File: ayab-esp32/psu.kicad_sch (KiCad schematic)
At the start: 45 parts, among them J602 Brother_5P, J604 Brother_4R, U401 XL1509, U402 XL1509

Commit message: Fix U602 3.3V regulator metadata [skip ci]
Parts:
- U402: LCSC ID C61063 -> C74193; OEM PN XL1509-5.0E1 -> XL1509-3.3E1
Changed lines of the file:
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@@
       (effects (font (size 1.27 1.27)) hide)
     )
-    (property "Datasheet" "https://datasheet.lcsc.com/lcsc/2304140030_XLSEMI-XL1509-5-0E1_C61063.pdf" (at 201.93 128.27 0)
+    (property "Datasheet" "https://www.lcsc.com/product-detail/C74193.html" (at 201.93 128.27 0)
       (effects (font (size 1.27 1.27)) hide)
     )
@@
       (effects (font (size 1.27 1.27)) hide)
     )
-    (property "LCSC ID" "C61063" (at 201.93 128.27 0)
+    (property "LCSC ID" "C74193" (at 201.93 128.27 0)
       (effects (font (size 1.27 1.27)) hide)
     )
-    (property "OEM PN" "XL1509-5.0E1" (at 201.93 128.27 0)
+    (property "OEM PN" "XL1509-3.3E1" (at 201.93 128.27 0)
       (effects (font (size 1.27 1.27)) hide)
     )

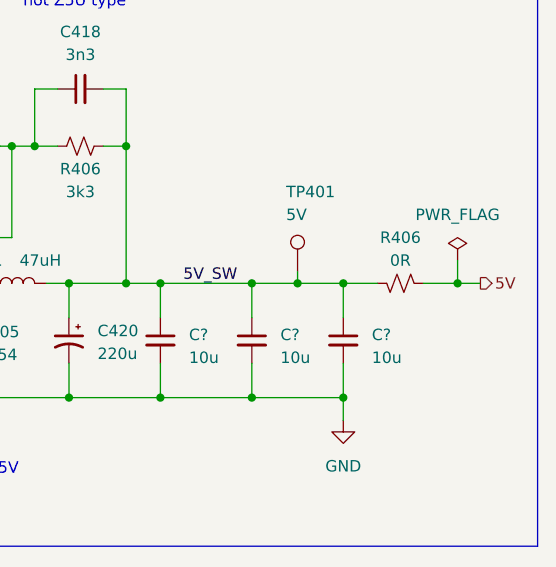
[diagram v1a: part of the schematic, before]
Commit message: Add LM66100 machine 5V reverse-current isolation
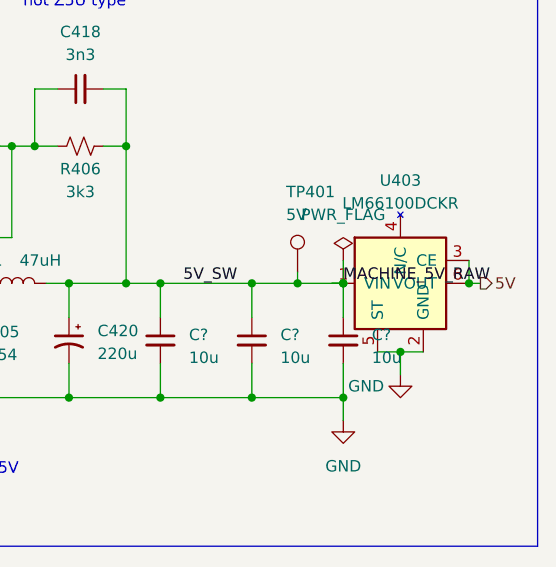
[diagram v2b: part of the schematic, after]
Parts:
- removed R406: 0R, Resistor_SMD:R_0603_1608Metric, symbol ayab-lib:R_Small_US
- added U403: LM66100DCKR, Package_TO_SOT_SMD:SOT-363_SC-70-6, symbol ayab-lib:LM66100
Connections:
- net 5V: now also U403.3 (CE), U403.6 (VOUT)
- net 5V_SW: now also U403.1 (VIN)
- net GND: now also U403.2 (GND), U403.5 (ST)
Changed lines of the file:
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@@
   )
   (junction (at 252.73 54.61) (diameter 0) (color 0 0 0 0)
-  )
-  (junction (at 270.51 54.61) (diameter 0) (color 0 0 0 0)
-  )
-  (junction (at 48.26 119.38) (diameter 0) (color 0 0 0 0)
+  )  (junction (at 48.26 119.38) (diameter 0) (color 0 0 0 0)
   )
   (junction (at 175.26 140.97) (diameter 0) (color 0 0 0 0)
@@
     (stroke (width 0) (type default))
   )
+  (wire (pts (xy 257.81 54.61) (xy 256.54 54.61))
+    (stroke (width 0) (type default))
+  )
+  (wire (pts (xy 257.81 52.07) (xy 257.81 54.61))
+    (stroke (width 0) (type default))
+  )
+  (wire (pts (xy 271.78 54.61) (xy 273.05 54.61))
+    (stroke (width 0) (type default))
+  )
+  (wire (pts (xy 271.78 52.07) (xy 271.78 54.61))
+    (stroke (width 0) (type default))
+  )
+  (wire (pts (xy 261.62 62.23) (xy 264.16 62.23))
+    (stroke (width 0) (type default))
+  )
+  (wire (pts (xy 266.7 62.23) (xy 264.16 62.23))
+    (stroke (width 0) (type default))
+  )
+  (wire (pts (xy 264.16 62.23) (xy 264.16 64.77))
+    (stroke (width 0) (type default))
+  )
+  (junction (at 257.81 54.61) (diameter 0) (color 0 0 0 0)
+  )
+  (junction (at 271.78 54.61) (diameter 0) (color 0 0 0 0)
+  )
+  (junction (at 264.16 62.23) (diameter 0) (color 0 0 0 0)
+  )
+  (label "MACHINE_5V_RAW" (at 257.81 54.61 0) (fields_autoplaced)
+    (effects (font (size 1.27 1.27)) (justify left bottom))
+  )
   (wire (pts (xy 115.57 54.61) (xy 109.22 54.61))
     (stroke (width 0) (type default))
@@
   (wire (pts (xy 203.2 67.31) (xy 205.74 67.31))
     (stroke (width 0) (type default))
-  )
-  (wire (pts (xy 270.51 52.07) (xy 270.51 54.61))
-    (stroke (width 0) (type default))
-  )
-  (wire (pts (xy 233.68 54.61) (xy 237.49 54.61))
+  )  (wire (pts (xy 233.68 54.61) (xy 237.49 54.61))
     (stroke (width 0) (type default))
   )
@@
   (wire (pts (xy 44.45 68.58) (xy 44.45 69.85))
     (stroke (width 0) (type default))
-  )
-  (wire (pts (xy 270.51 54.61) (xy 273.05 54.61))
-    (stroke (width 0) (type default))
-  )
-  (wire (pts (xy 237.49 67.31) (xy 247.65 67.31))
+  )  (wire (pts (xy 237.49 67.31) (xy 247.65 67.31))
     (stroke (width 0) (type default))
   )
@@
   (wire (pts (xy 252.73 54.61) (xy 257.81 54.61))
     (stroke (width 0) (type default))
-  )
-  (wire (pts (xy 266.7 54.61) (xy 270.51 54.61))
-    (stroke (width 0) (type default))
-  )
-  (wire (pts (xy 110.49 120.65) (xy 110.49 123.19))
+  )  (wire (pts (xy 110.49 120.65) (xy 110.49 123.19))
     (stroke (width 0) (type default))
   )
@@
   (wire (pts (xy 110.49 113.03) (xy 110.49 115.57))
     (stroke (width 0) (type default))
-  )
-  (wire (pts (xy 257.81 54.61) (xy 261.62 54.61))
-    (stroke (width 0) (type default))
-  )
-  (wire (pts (xy 189.23 67.31) (xy 198.12 67.31))
+  )  (wire (pts (xy 189.23 67.31) (xy 198.12 67.31))
     (stroke (width 0) (type default))
   )
@@
     )
   )
-  (symbol (lib_id "ayab-lib:R_Small_US") (at 264.16 54.61 90) (mirror x) (unit 1)
-    (in_bom yes) (on_board yes) (dnp no)
-    (property "Reference" "R406" (at 264.16 49.53 90)
-      (effects (font (size 1.27 1.27)))
-    )
-    (property "Value" "0R" (at 264.16 52.07 90)
-      (effects (font (size 1.27 1.27)))
-    )
-    (property "Footprint" "Resistor_SMD:R_0603_1608Metric" (at 264.16 54.61 0)
-      (effects (font (size 1.27 1.27)) hide)
-    )
-    (property "Datasheet" "~" (at 264.16 54.61 0)
-      (effects (font (size 1.27 1.27)) hide)
-    )
-    (property "Package" "0603" (at 264.16 54.61 0)
-      (effects (font (size 1.27 1.27)) hide)
-    )
-    (property "LCSC ID" "C21189" (at 264.16 54.61 0)
-      (effects (font (size 1.27 1.27)) hide)
-    )
-    (property "OEM PN" "0603WAF0000T5E" (at 264.16 54.61 0)
-      (effects (font (size 1.27 1.27)) hide)
-    )
-    (property "OEM" "UNI-ROYAL(Uniroyal Elec)" (at 264.16 54.61 0)
-      (effects (font (size 1.27 1.27)) hide)
-    )
-    (pin "1")
-    (pin "2")
-    (instances
-      (project "electronic-knitter"
-        (path "/a3f4eded-ecb9-44ce-82ad-ad815e00f2c9/d37dfdc2-398a-4de1-8840-934586e4e3cf"
-          (reference "R406") (unit 1)
-        )
-      )
-      (project "ayab-esp32"
-        (path "/ad16b75f-afc8-4717-a7c6-8dd7b69a18e2/512b1de4-f8f4-4173-a7be-69b46f59a5e5"
-          (reference "R611") (unit 1)
-        )
-      )
-    )
-  )
   (symbol (lib_id "power:+3V3") (at 133.35 113.03 0) (unit 1)
     (in_bom yes) (on_board yes) (dnp no) (fields_autoplaced)
@@
     )
   )
-  (symbol (lib_id "power:PWR_FLAG") (at 270.51 52.07 0) (unit 1)
+  (symbol (lib_id "power:PWR_FLAG") (at 257.81 52.07 0) (unit 1)
     (in_bom yes) (on_board yes) (dnp no) (fields_autoplaced)
-    (property "Reference" "#FLG0605" (at 270.51 50.165 0)
+    (property "Reference" "#FLG0605" (at 257.81 50.165 0)
       (effects (font (size 1.27 1.27)) hide)
     )
-    (property "Value" "PWR_FLAG" (at 270.51 46.99 0)
+    (property "Value" "PWR_FLAG" (at 257.81 46.99 0)
       (effects (font (size 1.27 1.27)))
     )
-    (property "Footprint" "" (at 270.51 52.07 0)
+    (property "Footprint" "" (at 257.81 52.07 0)
       (effects (font (size 1.27 1.27)) hide)
     )
-    (property "Datasheet" "~" (at 270.51 52.07 0)
+    (property "Datasheet" "~" (at 257.81 52.07 0)
       (effects (font (size 1.27 1.27)) hide)
     )
@@
         )
       )
+    )
+  )
+  (symbol (lib_id "ayab-lib:LM66100") (at 264.16 54.61 0) (unit 1)
+    (in_bom yes) (on_board yes) (dnp no) (fields_autoplaced)
+    (property "Reference" "U403" (at 264.16 43.18 0)
+      (effects (font (size 1.27 1.27)))
+    )
+    (property "Value" "LM66100DCKR" (at 264.16 45.72 0)
+      (effects (font (size 1.27 1.27)))
+    )
+    (property "Footprint" "Package_TO_SOT_SMD:SOT-363_SC-70-6" (at 264.16 54.61 0)
+      (effects (font (size 1.27 1.27)) hide)
+    )
+    (property "Datasheet" "https://www.ti.com/lit/ds/symlink/lm66100.pdf" (at 264.16 54.61 0)
+      (effects (font (size 1.27 1.27)) hide)
+    )
+    (property "Package" "SC-70-6" (at 264.16 54.61 0)
+      (effects (font (size 1.27 1.27)) hide)
+    )
+    (property "LCSC ID" "C2869734" (at 264.16 54.61 0)
+      (effects (font (size 1.27 1.27)) hide)
+    )
+    (property "OEM PN" "LM66100DCKR" (at 264.16 54.61 0)
+      (effects (font (size 1.27 1.27)) hide)
+    )
+    (property "OEM" "Texas Instruments" (at 264.16 54.61 0)
+      (effects (font (size 1.27 1.27)) hide)
+    )
+    (pin "1")
+    (pin "2")
+    (pin "3")
+    (pin "4")
+    (pin "5")
+    (pin "6")
+    (instances
+      (project "electronic-knitter"
+        (path "/a3f4eded-ecb9-44ce-82ad-ad815e00f2c9/d37dfdc2-398a-4de1-8840-934586e4e3cf"
+          (reference "U403") (unit 1)
+        )
+      )
+      (project "ayab-esp32"
+        (path "/ad16b75f-afc8-4717-a7c6-8dd7b69a18e2/512b1de4-f8f4-4173-a7be-69b46f59a5e5"
+          (reference "U403") (unit 1)
+        )
+      )
+    )
+  )
+(symbol (lib_id "power:GND") (at 264.16 64.77 0) (unit 1)
+    (in_bom yes) (on_board yes) (dnp no)
+    (property "Reference" "#PWR720" (at 264.16 71.12 0)
+      (effects (font (size 1.27 1.27)) hide)
+    )
+    (property "Value" "GND" (at 260.35 66.04 0)
+      (effects (font (size 1.27 1.27)))
+    )
+    (property "Footprint" "" (at 264.16 64.77 0)
+      (effects (font (size 1.27 1.27)) hide)
+    )
+    (property "Datasheet" "" (at 264.16 64.77 0)
+      (effects (font (size 1.27 1.27)) hide)
+    )
+    (pin "1")
+    (instances
+      (project "electronic-knitter"
+        (path "/a3f4eded-ecb9-44ce-82ad-ad815e00f2c9/d37dfdc2-398a-4de1-8840-934586e4e3cf"
+          (reference "#PWR720") (unit 1)
+        )
+      )
+      (project "ayab-esp32"
+        (path "/ad16b75f-afc8-4717-a7c6-8dd7b69a18e2/512b1de4-f8f4-4173-a7be-69b46f59a5e5"
+          (reference "#PWR0609") (unit 1)
+        )
+      )

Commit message: Close Rev A independent audit repair order
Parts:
- D601: symbol Device:D_Bridge_+-AA -> ayab-lib:KMB14F_Bridge
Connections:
- net +12V: no longer C?.1, C?.1, C?.1
- new net SOLENOID_12V_SW: C?.1, C?.1, C?.1
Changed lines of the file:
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@@
   (junction (at 264.16 62.23) (diameter 0) (color 0 0 0 0)
   )
-  (label "MACHINE_5V_RAW" (at 257.81 54.61 0) (fields_autoplaced)
-    (effects (font (size 1.27 1.27)) (justify left bottom))
-  )
   (wire (pts (xy 115.57 54.61) (xy 109.22 54.61))
     (stroke (width 0) (type default))
@@
     (stroke (width 0) (type default))
   )
-  (wire (pts (xy 26.67 119.38) (xy 38.1 119.38))
-    (stroke (width 0) (type default))
-  )
   (wire (pts (xy 67.31 49.53) (xy 71.12 49.53))
     (stroke (width 0) (type default))
@@
     (stroke (width 0) (type default))
   )
-  (wire (pts (xy 58.42 119.38) (xy 68.58 119.38))
-    (stroke (width 0) (type default))
-  )
   (wire (pts (xy 247.65 140.97) (xy 257.81 140.97))
     (stroke (width 0) (type default))
@@
     (effects (font (size 1.27 1.27)) (justify left bottom))
   )
-  (label "BRIDGE_P" (at 71.12 36.83 0) (fields_autoplaced)
-    (effects (font (size 1.27 1.27)) (justify left bottom))
-  )
   (label "5V_SW" (at 240.03 54.61 0) (fields_autoplaced)
     (effects (font (size 1.27 1.27)) (justify left bottom))
@@
     )
   )
-  (symbol (lib_id "Device:D_Bridge_+-AA") (at 59.69 49.53 0) (unit 1)
+  (symbol (lib_id "ayab-lib:KMB14F_Bridge") (at 59.69 49.53 0) (unit 1)
     (in_bom yes) (on_board yes) (dnp no)
     (property "Reference" "D601" (at 64.77 54.61 0)
@@
     )
   )
+  (global_label "SOLENOID_12V_SW" (shape input) (at 48.26 119.38 0) (fields_autoplaced)
+    (effects (font (size 1.27 1.27)) (justify left))
+  )
+  (global_label "+12V" (shape input) (at 68.58 119.38 0) (fields_autoplaced)
+    (effects (font (size 1.27 1.27)) (justify left))
+  )
 )

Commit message: Close final Rev A preorder audit findings
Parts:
- D405, D406: OEM (none) -> MDD (Microdiode Semiconductor)
- D601: Package (none) -> MBF
- gave numbers to parts that had none: 14
